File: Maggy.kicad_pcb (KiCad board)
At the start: 2 copper layers, 160 x 100 mm, 125 parts, among them J1 XY308-2.54-2P, J2 XY308-2.54-2P, J3 XY308-2.54-2P, J4 XY308-2.54-2P, U1 CH224K, U10 INA214AIDCKR, U11 Socket for Teensy 4.1 (2x 1x2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, U12 INA214AIDCKR, U13 INA214AIDCKR, U14 TMAG5170A2DGKR, U15 TMAG5170A2DGKR, U16 TMAG5170A2DGKR, U17 TMAG5170A2DGKR, U18 TMAG5170A2DGKR, U2 A4950ELJTR-T, U3 A4950ELJTR-T, U4 A4950ELJTR-T, U5 A4950ELJTR-T, U6 TLV2372, U7 LM1117S-3.3, U8 LM1117S-5.0, U9 INA214AIDCKR

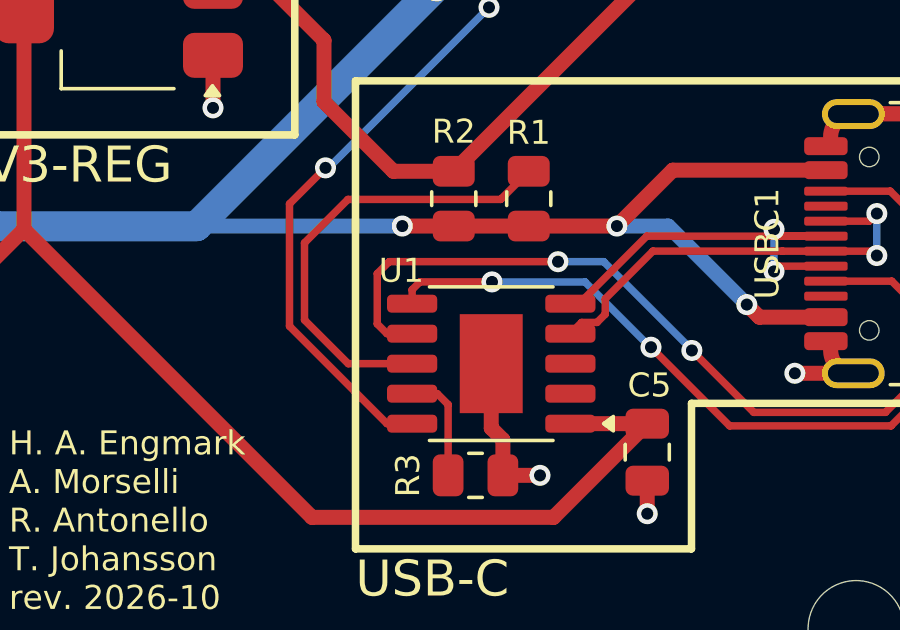
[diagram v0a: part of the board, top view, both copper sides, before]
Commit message: fix: update LED resistor values
LED resistors values were too low to comply with the stated limits in the
datasheet. They draw too much continuous current, exceeding the 20mA.
Updated resistor so current draw is limited to about 5-6mA.

Also updated the LEDs themselves to ensure they all reference the same
component and datasheet.
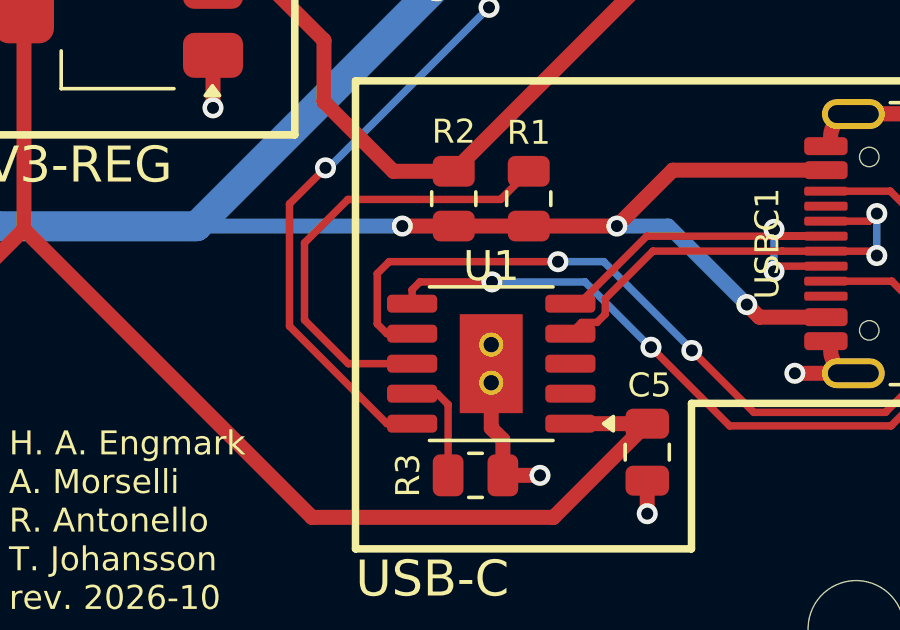
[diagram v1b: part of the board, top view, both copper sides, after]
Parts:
- LED1, LED2, LED3, LED4: value Yellow-Green -> XL-1608SYGC-06
- R12: value 120 -> 470
- R13, R4: value 56 -> 220
- U1: footprint Package_SO:SSOP-10-1EP_3.9x4.9mm_P1mm_EP2.1x3.3mm -> Package_SO:SSOP-10-1EP_3.9x4.9mm_P1mm_EP2.1x3.3mm_ThermalVias
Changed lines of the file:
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@@
 			)
 		)
-		(property "Value" "Yellow-Green"
+		(property "Value" "XL-1608SYGC-06"
 			(at 0 1.43 0)
 			(layer "F.Fab")
@@
 			)
 		)
-		(property "Value" "Yellow-Green"
+		(property "Value" "XL-1608SYGC-06"
 			(at 0 1.43 0)
 			(layer "F.Fab")
@@
 			)
 		)
-		(property "Datasheet" "https://atta.szlcsc.com/upload/public/pdf/source/20221102/D860AFDD1CDB02C5A8064103A32707E2.pdf"
+		(property "Datasheet" "https://www.lcsc.com/datasheet/C965805.pdf"
 			(at 0 0 0)
 			(layer "F.Fab")
@@
 			)
 		)
-		(property "Manufacturer Part" "XL-1608SURC-06"
+		(property "Manufacturer Part" "XL-1608SYGC-06"
 			(at 0 0 0)
 			(unlocked yes)
@@
 			)
 		)
-		(property "Supplier Part" "C965799"
+		(property "Supplier Part" "C965805"
 			(at 0 0 0)
 			(unlocked yes)
@@
 			)
 		)
-		(property "LCSC Part Name" "XL-1608SURC-06"
+		(property "LCSC Part Name" "XL-1608SYGC-06"
 			(at 0 0 0)
 			(unlocked yes)
@@
 			)
 		)
-		(property "Value" "Yellow-Green"
+		(property "Value" "XL-1608SYGC-06"
 			(at 0 1.43 0)
 			(layer "F.Fab")
@@
 			)
 		)
-		(property "Datasheet" "https://atta.szlcsc.com/upload/public/pdf/source/20221102/F362183196D461585F90F08511E6DE2E.pdf"
+		(property "Datasheet" "https://www.lcsc.com/datasheet/C965805.pdf"
 			(at 0 0 0)
 			(layer "F.Fab")
@@
 			)
 		)
-		(property "Value" "Yellow-Green"
+		(property "Value" "XL-1608SYGC-06"
 			(at 0 1.43 0)
 			(layer "F.Fab")
@@
 			)
 		)
-		(property "Datasheet" "https://atta.szlcsc.com/upload/public/pdf/source/20221102/F362183196D461585F90F08511E6DE2E.pdf"
+		(property "Datasheet" "https://www.lcsc.com/datasheet/C965805.pdf"
 			(at 0 0 0)
 			(layer "F.Fab")
@@
 			)
 		)
-		(property "Value" "56"
+		(property "Value" "220"
 			(at 0 1.65 180)
 			(layer "F.Fab")
@@
 			)
 		)
-		(property "Value" "120"
+		(property "Value" "470"
 			(at 0 1.65 0)
 			(layer "F.Fab")
@@
 			)
 		)
-		(property "Value" "56"
+		(property "Value" "220"
 			(at 0 1.65 0)
 			(layer "F.Fab")
@@
 		)
 	)
-	(footprint "Package_SO:SSOP-10-1EP_3.9x4.9mm_P1mm_EP2.1x3.3mm"
+	(footprint "Package_SO:SSOP-10-1EP_3.9x4.9mm_P1mm_EP2.1x3.3mm_ThermalVias"
 		(layer "F.Cu")
 		(at 210.925 144.027297 180)
@@
 		(tags "SSOP SO ESSOP-10")
 		(property "Reference" "U1"
-			(at 3 3.1 0)
+			(at 0 3.25 180)
 			(layer "F.SilkS")
 			(effects
 				(font
-					(size 0.8 0.8)
+					(size 1 1)
 					(thickness 0.15)
 				)
@@
 		)
 		(property "Value" "CH224K"
-			(at 0 3.4 0)
+			(at 0 3.4 180)
 			(layer "F.Fab")
-			(hide yes)
 			(effects
 				(font
@@
 		)
 		(property "Datasheet" "https://www.wch.cn/downloads/file/301.html"
-			(at 0 0 0)
+			(at 0 0 180)
 			(layer "F.Fab")
 			(hide yes)
@@
 		)
 		(property "Description" "100W USB Type-C PD3.0/2.0, BC1.2 Sink Controller, SSOP-10"
-			(at 0 0 0)
+			(at 0 0 180)
 			(layer "F.Fab")
 			(hide yes)
@@
 		)
 		(property "KiLib_Generator" "package/gullwing"
-			(at 0 0 0)
+			(at 0 0 180)
 			(layer "F.SilkS")
 			(hide yes)
@@
 			)
 		)
-		(property "JLC_3D_Size" "4.9 6"
-			(at 0 0 0)
-			(layer "Cmts.User")
+		(property "Manufacturer Part" "CH224K"
+			(at 0 0 180)
+			(unlocked yes)
+			(layer "F.Fab")
 			(hide yes)
 			(effects
 				(font
-					(size 1.27 1.27)
+					(size 1 1)
 					(thickness 0.15)
 				)
 			)
 		)
-		(property "Manufacturer Part" "CH224K"
+		(property "Manufacturer" "WCH(南京沁恒)"
 			(at 0 0 180)
 			(unlocked yes)
@@
 			)
 		)
-		(property "Manufacturer" "WCH(南京沁恒)"
+		(property "Supplier Part" "C970725"
 			(at 0 0 180)
 			(unlocked yes)
@@
 			)
 		)
-		(property "Supplier Part" "C970725"
+		(property "Supplier" "LCSC"
 			(at 0 0 180)
 			(unlocked yes)
@@
 			)
 		)
-		(property "Supplier" "LCSC"
+		(property "LCSC Part Name" "USB PD等多快充协议受电芯片CH224"
 			(at 0 0 180)
 			(unlocked yes)
@@
 			)
 		)
-		(property "LCSC Part Name" "USB PD等多快充协议受电芯片CH224"
+		(property "JLC_3D_Size" "4.9 6"
 			(at 0 0 180)
 			(unlocked yes)
@@
 		)
 		(fp_text user "${REFERENCE}"
-			(at 0 0 90)
+			(at 0 0 270)
 			(layer "F.Fab")
 			(effects
 				(font
-					(size 0.8 0.8)
+					(size 1 1)
 					(thickness 0.15)
 				)
@@
 			(pintype "open_collector")
 		)
+		(pad "11" thru_hole circle
+			(at 0 -0.635 180)
+			(size 0.81 0.81)
+			(drill 0.51)
+			(property pad_prop_heatsink)
+			(layers "*.Cu")
+			(remove_unused_layers no)
+			(net "GND")
+			(pinfunction "GND_11")
+			(pintype "power_in")
+		)
+		(pad "11" smd rect
+			(at 0 0 180)
+			(size 0.81 2.08)
+			(property pad_prop_heatsink)
+			(layers "B.Cu")
+			(net "GND")
+			(pinfunction "GND_11")
+			(pintype "power_in")
+			(zone_connect 2)
+		)
 		(pad "11" smd rect
 			(at 0 0 180)
@@
 			(zone_connect 2)
 		)
+		(pad "11" thru_hole circle
+			(at 0 0.635 180)
+			(size 0.81 0.81)
+			(drill 0.51)
+			(property pad_prop_heatsink)
+			(layers "*.Cu")
+			(remove_unused_layers no)
+			(net "GND")
+			(pinfunction "GND_11")
+			(pintype "power_in")
+		)
 		(embedded_fonts no)

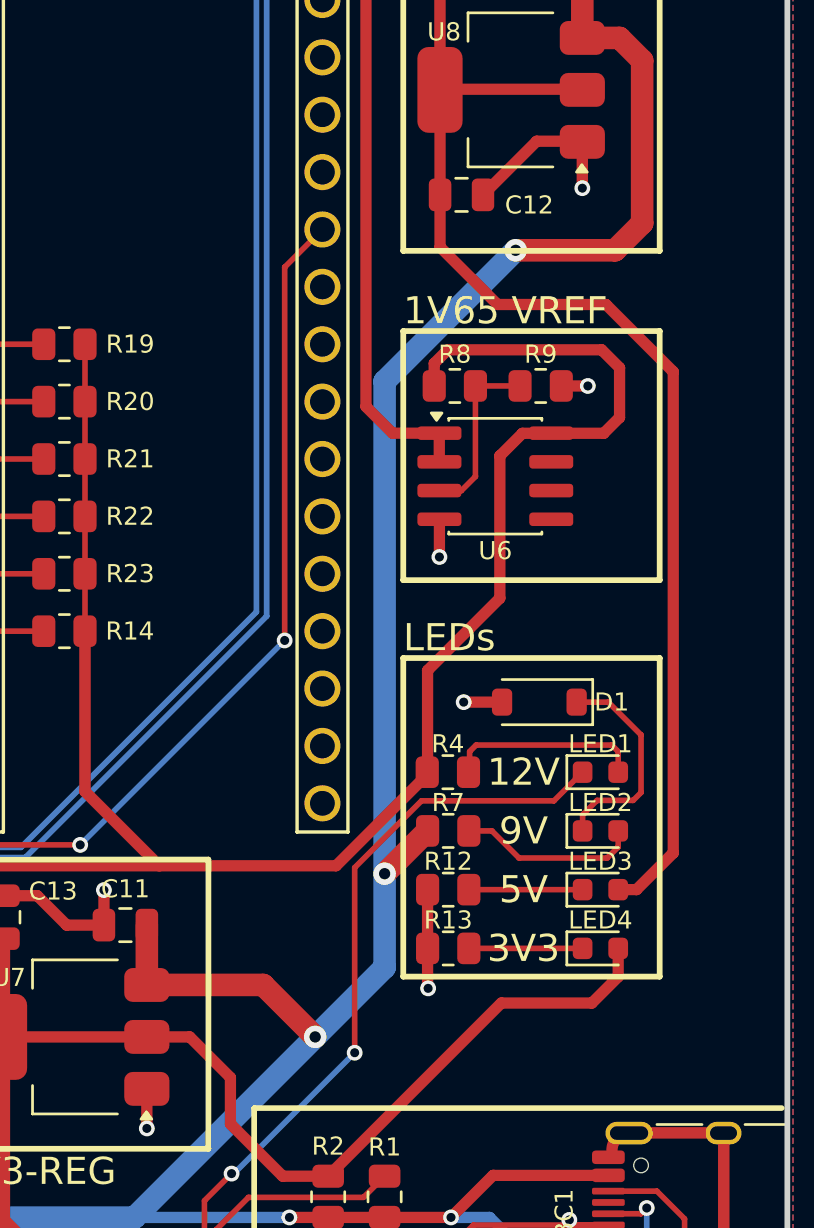
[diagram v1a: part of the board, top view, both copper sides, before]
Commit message: refactor(power): cascade 3V3 regulator input from +5V rail instead of 12V VBUS
- Connect LM1117-3.3 VIN to regulated +5V output rather than raw 12V VBUS.
  This matches the design from board version 4.3, and should provide improved
  LDO PSRR (power supply rejection ratio) to isolate 12V solenoid PWM
  switching noise from the +3V3 rail. The +3V3 rail is connected to things like
  the +1V65 current sense reference, and should be as stable as possible.
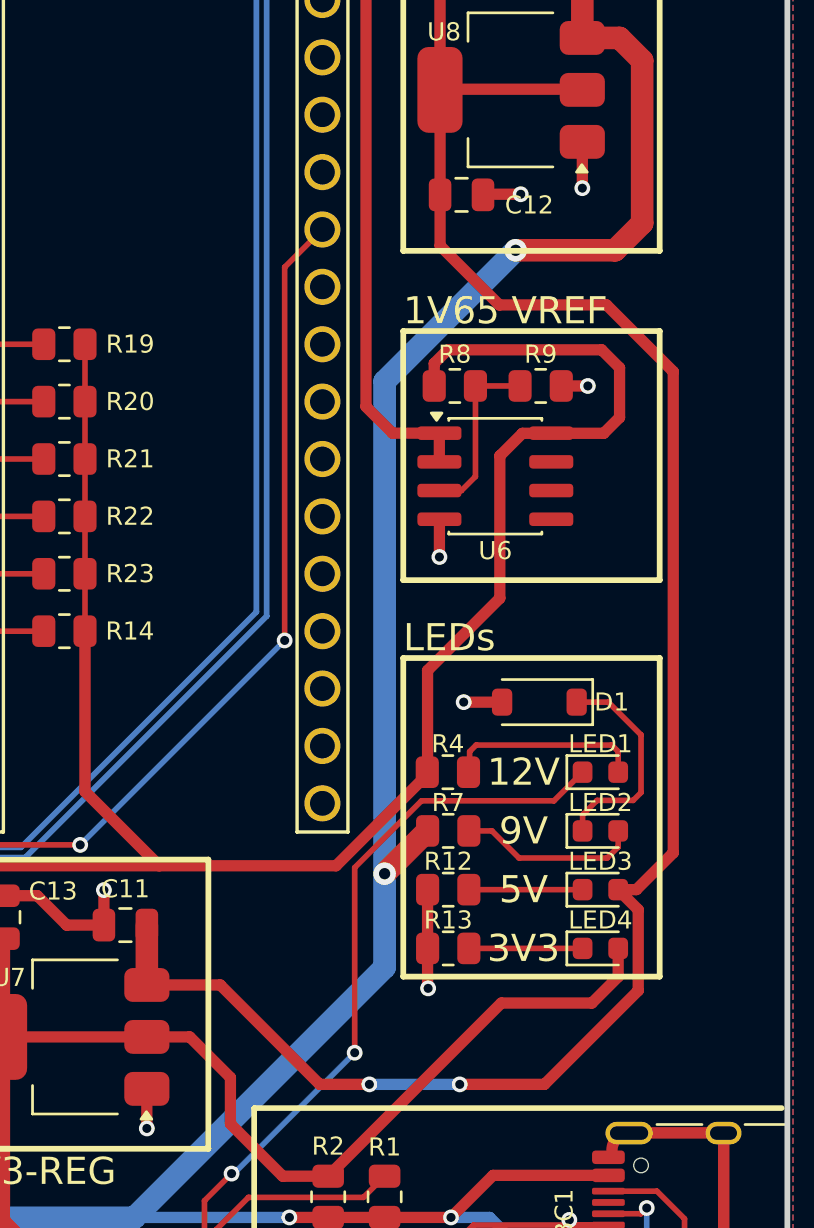
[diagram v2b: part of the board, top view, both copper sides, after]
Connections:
- C11 pad 2: VBUS -> +5V
- U7 pad 3: VBUS -> +5V
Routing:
- net +5V: track 81.0 -> 113.8 mm, vias 0 -> 2
- net VBUS: track 248.4 -> 237.3 mm, vias 10 -> 9
- net GND: track 410.0 -> 406.3 mm, vias 30 -> 31
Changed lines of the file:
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@@
 			(layers "F.Cu" "F.Mask" "F.Paste")
 			(roundrect_rratio 0.25)
-			(net "VBUS")
+			(net "+5V")
 			(pintype "passive")
 		)
@@
 			(layers "F.Cu" "F.Mask" "F.Paste")
 			(roundrect_rratio 0.25)
-			(net "VBUS")
+			(net "+5V")
 			(pinfunction "VI_3")
 			(pintype "power_in")
@@
 	)
 	(segment
+		(start 216.5565 94.15)
+		(end 216.529 94.1775)
+		(width 0.5)
+		(layer "F.Cu")
+		(net "GND")
+	)
+	(segment
 		(start 185.0945 92.943)
 		(end 178.2 92.943)
@@
 	)
 	(segment
-		(start 216.529 94.17725)
-		(end 218.90375 91.8025)
-		(width 0.5)
-		(layer "F.Cu")
-		(net "GND")
-	)
-	(segment
 		(start 121.838344 109.25425)
 		(end 121.535081 108.679331)
@@
 	)
 	(segment
-		(start 218.90375 91.8025)
-		(end 220.954 91.8025)
-		(width 0.5)
-		(layer "F.Cu")
-		(net "GND")
-	)
-	(segment
 		(start 217.375 116.63125)
 		(end 215.675 116.63125)
@@
 	)
 	(segment
-		(start 216.529 94.1775)
-		(end 216.529 94.17725)
-		(width 0.5)
-		(layer "F.Cu")
-		(net "GND")
-	)
-	(segment
 		(start 186.795 84.92)
 		(end 181.135 84.92)
@@
 	)
 	(segment
+		(start 218.2 94.15)
+		(end 216.5565 94.15)
+		(width 0.5)
+		(layer "F.Cu")
+		(net "GND")
+	)
+	(segment
 		(start 128.914256 105.521761)
 		(end 128.610994 104.946841)
@@
 	)
 	(via
+		(at 218.2 94.15)
+		(size 0.7)
+		(drill 0.4)
+		(layers "F.Cu" "B.Cu")
+		(net "GND")
+	)
+	(via
 		(at 74 81.6)
 		(size 0.61)
@@
 	)
 	(segment
-		(start 209.1 131.45)
-		(end 206.8 129.15)
-		(width 1)
-		(layer "F.Cu")
-		(net "VBUS")
-	)
-	(segment
 		(start 177.061 89.961)
 		(end 178.557 91.457)
@@
 	)
 	(segment
-		(start 201.65 126.5)
-		(end 201.65 129.15)
-		(width 1)
-		(layer "F.Cu")
-		(net "VBUS")
-	)
-	(segment
 		(start 181.3045 89.4955)
 		(end 181.3045 91.369)
@@
 	)
 	(segment
-		(start 206.8 129.15)
-		(end 201.65 129.15)
-		(width 1)
-		(layer "F.Cu")
-		(net "VBUS")
-	)
-	(segment
 		(start 186.225 104.703)
 		(end 184.5665 104.703)
@@
 	)
 	(via
-		(at 209.1 131.45)
-		(size 1)
-		(drill 0.5)
-		(layers "F.Cu" "B.Cu")
-		(net "VBUS")
-	)
-	(via
 		(at 215.1125 139.439797)
 		(size 0.7)
@@
 	)
 	(segment
+		(start 211.5 133.55)
+		(end 209.3 133.55)
+		(width 0.5)
+		(layer "F.Cu")
+		(net "+5V")
+	)
+	(segment
+		(start 214.629 96.429)
+		(end 214.629 94.1775)
+		(width 0.5)
+		(layer "F.Cu")
+		(net "+5V")
+	)
+	(segment
 		(start 220.954 89.5025)
 		(end 214.654 89.5025)
@@
 	)
 	(segment
+		(start 219.25 133.55)
+		(end 215.5 133.55)
+		(width 0.5)
+		(layer "F.Cu")
+		(net "+5V")
+	)
+	(segment
+		(start 222.5125 124.93125)
+		(end 223.31875 124.93125)
+		(width 0.5)
+		(layer "F.Cu")
+		(net "+5V")
+	)
+	(segment
 		(start 209.541 62.654)
 		(end 209.439 62.654)
@@
 	)
 	(segment
-		(start 214.629 96.48525)
-		(end 214.629 94.1775)
+		(start 209.3 133.55)
+		(end 204.9 129.15)
+		(width 0.5)
+		(layer "F.Cu")
+		(net "+5V")
+	)
+	(segment
+		(start 204.9 129.15)
+		(end 201.65 129.15)
 		(width 0.5)
 		(layer "F.Cu")
@@
 	)
 	(segment
-		(start 222.5125 124.93125)
-		(end 223.325 124.93125)
+		(start 222 99.05)
+		(end 217.25 99.05)
 		(width 0.5)
 		(layer "F.Cu")
@@
 	)
 	(segment
-		(start 223.325 124.93125)
-		(end 224.95 123.30625)
-		(width 0.5)
+		(start 201.65 126.5)
+		(end 201.65 129.15)
+		(width 1)
 		(layer "F.Cu")
 		(net "+5V")
@@
 	)
 	(segment
-		(start 224.95 102.00625)
-		(end 221.975 99.03125)
+		(start 224.95 123.3)
+		(end 224.95 102)
 		(width 0.5)
 		(layer "F.Cu")
@@
 	)
 	(segment
-		(start 221.975 99.03125)
-		(end 217.175 99.03125)
+		(start 223.31875 124.93125)
+		(end 224.95 123.3)
+		(width 0.5)
+		(layer "F.Cu")
+		(net "+5V")
+	)
+	(segment
+		(start 222.5125 124.93125)
+		(end 223.4 125.81875)
+		(width 0.5)
+		(layer "F.Cu")
+		(net "+5V")
+	)
+	(segment
+		(start 223.4 125.81875)
+		(end 223.4 129.4)
 		(width 0.5)
 		(layer "F.Cu")
@@
 	)
 	(segment
-		(start 217.175 99.03125)
-		(end 214.629 96.48525)
+		(start 223.4 129.4)
+		(end 219.25 133.55)
+		(width 0.5)
+		(layer "F.Cu")
+		(net "+5V")
+	)
+	(segment
+		(start 224.95 102)
+		(end 222 99.05)
 		(width 0.5)
 		(layer "F.Cu")
@@
 	)
 	(segment
-		(start 224.95 123.30625)
-		(end 224.95 102.00625)
+		(start 217.25 99.05)
+		(end 214.629 96.429)
 		(width 0.5)
 		(layer "F.Cu")
@@
 		(net "+5V")
 	)
+	(via
+		(at 211.5 133.55)
+		(size 0.7)
+		(drill 0.4)
+		(layers "F.Cu" "B.Cu")
+		(net "+5V")
+	)
+	(via
+		(at 215.5 133.55)
+		(size 0.7)
+		(drill 0.4)
+		(layers "F.Cu" "B.Cu")
+		(net "+5V")
+	)
+	(segment
+		(start 215.5 133.55)
+		(end 211.5 133.55)
+		(width 0.5)
+		(layer "B.Cu")
+		(net "+5V")
+	)

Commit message: chore: update 9V LED resistor
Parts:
- R7: value 200 -> 750
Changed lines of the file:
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@@
 			)
 		)
-		(property "Value" "200"
+		(property "Value" "750"
 			(at 0 1.65 180)
 			(layer "F.Fab")
@@
 			)
 		)
-		(property "Description" "Resistor"
+		(property "Description" "Rset"
 			(at 0 0 0)
 			(layer "F.Fab")

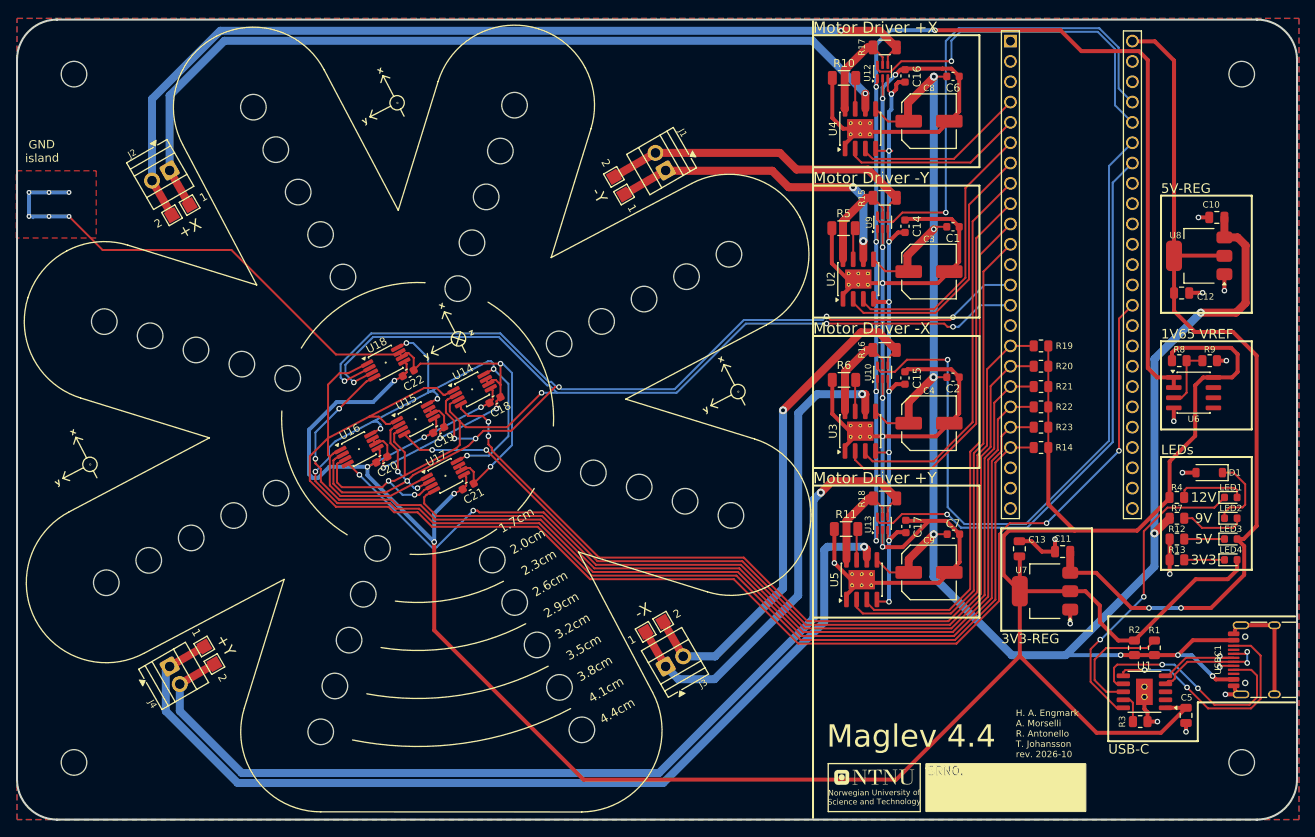
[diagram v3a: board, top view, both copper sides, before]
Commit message: chore: replace the top 3V3 with a GND plane
Between revisions 4.2 and 4.3 this change was introduced in order to give more shielding to the I2C bus lines from the changing magnetic fields, so it has now been introduced here as well, even though the impact it will have on shielding the SPI bus lines is dubious.
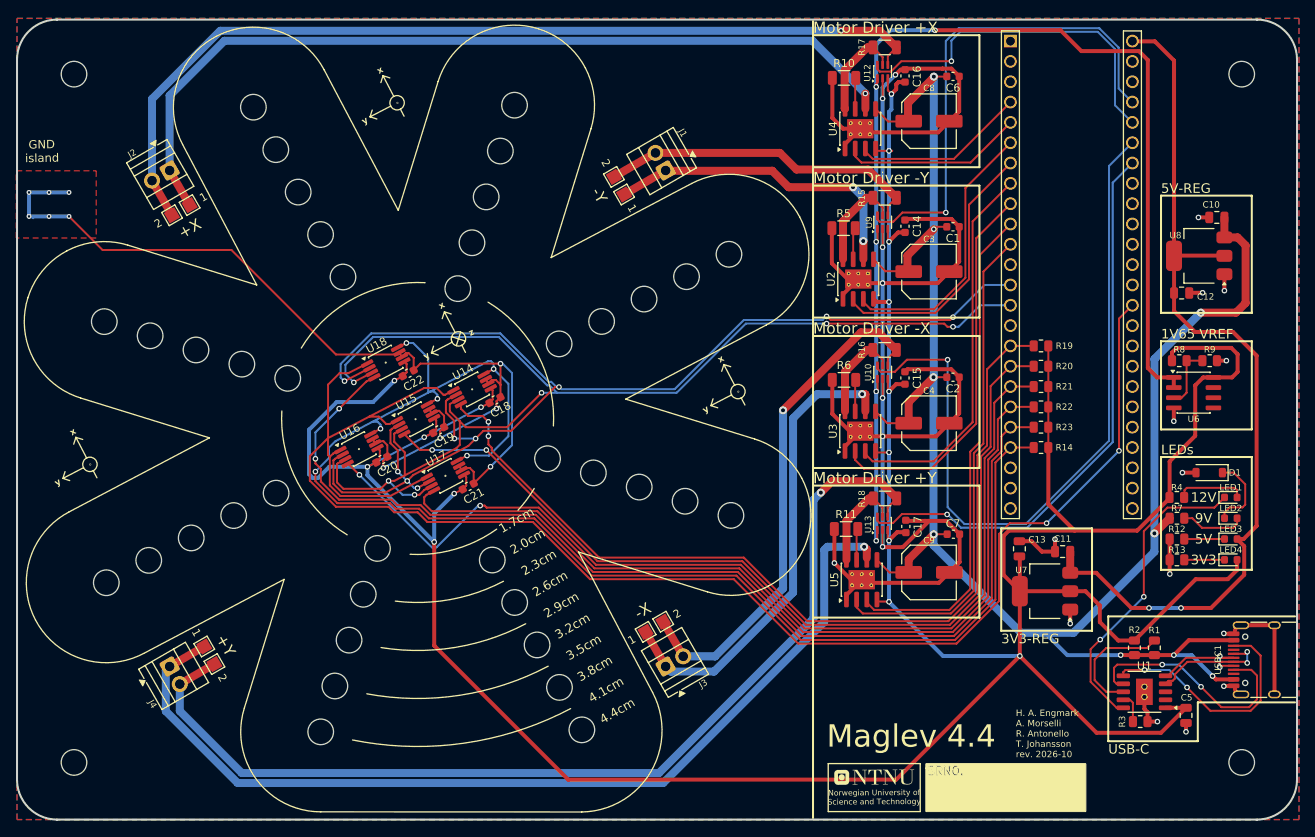
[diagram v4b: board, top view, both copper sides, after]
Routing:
- net +3V3: track 432.3 -> 452.6 mm, vias 14 -> 15
- net VBUS: track 237.3 -> 235.9 mm
- net 4_1: track 61.3 -> 59.9 mm
- net GND: track 406.3 -> 406.9 mm, vias 31 -> 32
- net SPI_CS_3: track 124.0 -> 124.5 mm
- removed copper zone on F.Cu, net +3V3

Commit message: chore: simplify and move ground island
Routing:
- net GND: track 406.9 -> 345.5 mm, vias 32 -> 26
